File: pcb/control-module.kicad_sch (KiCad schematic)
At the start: 22 parts, among them J1 Screw_Terminal_01x06, J2 Conn_01x07_Pin, SW1 SW_DIP_x04, U1 TC2185-3.3VxCTTR

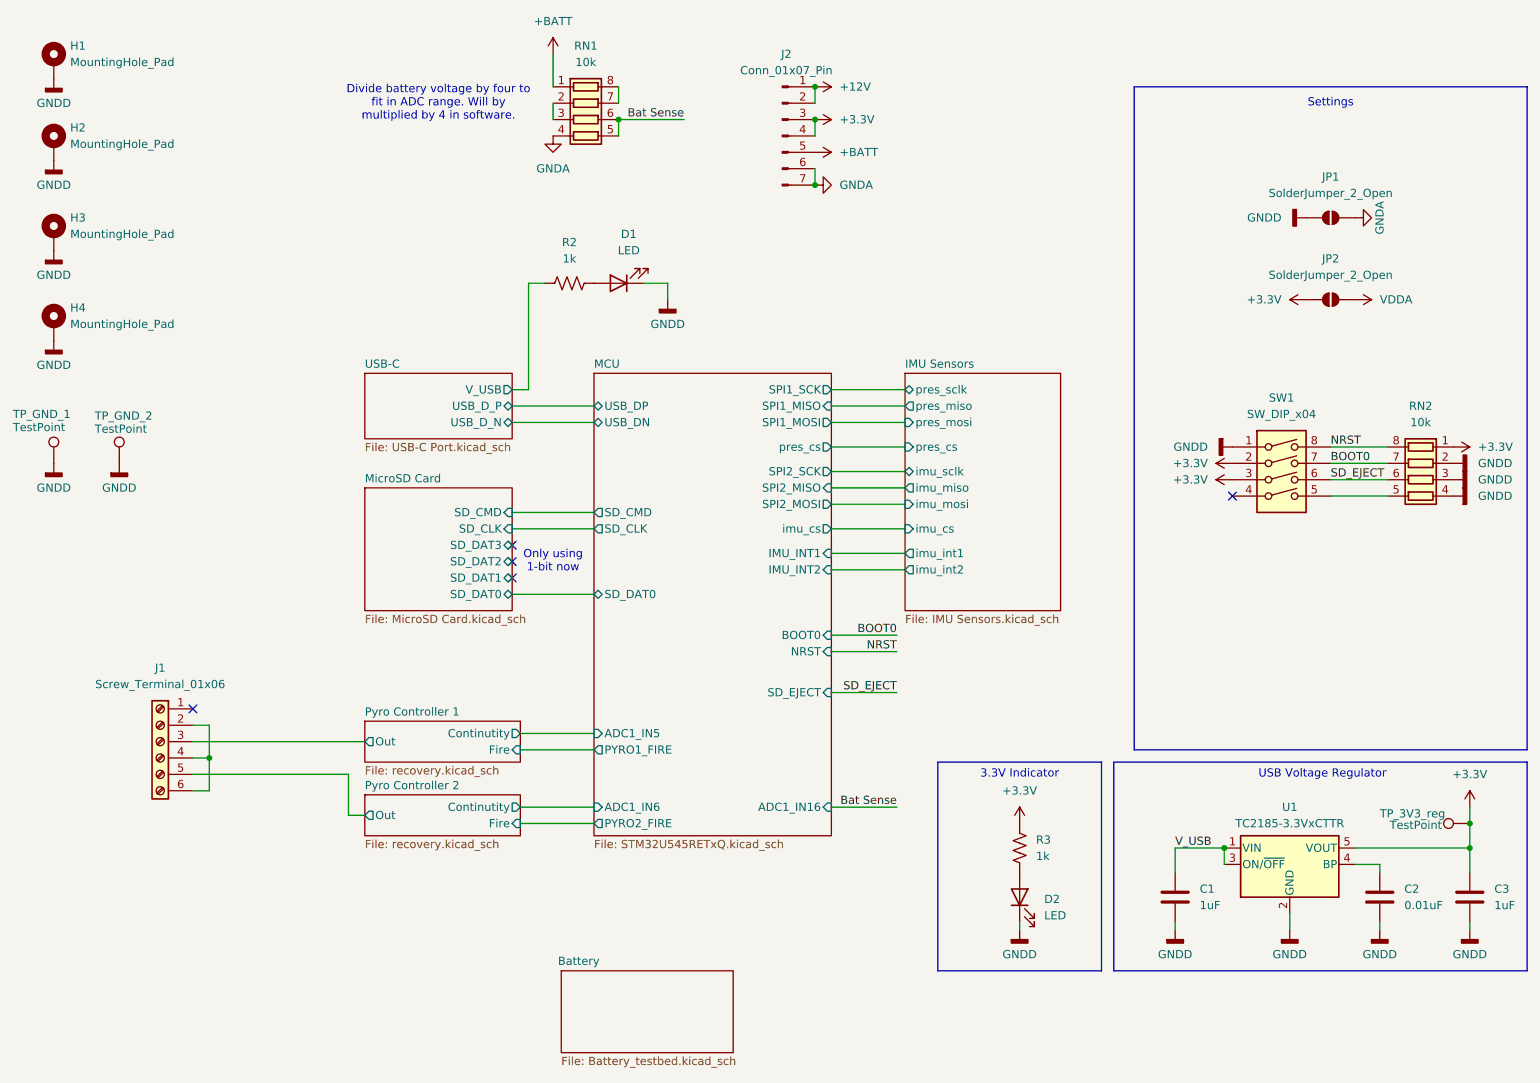
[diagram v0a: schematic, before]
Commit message: Updated Control Mod test bed schematics
finished testpoints, got rid of Vbus and replaced with +5V, added +3.3v to pyro J1 terminal
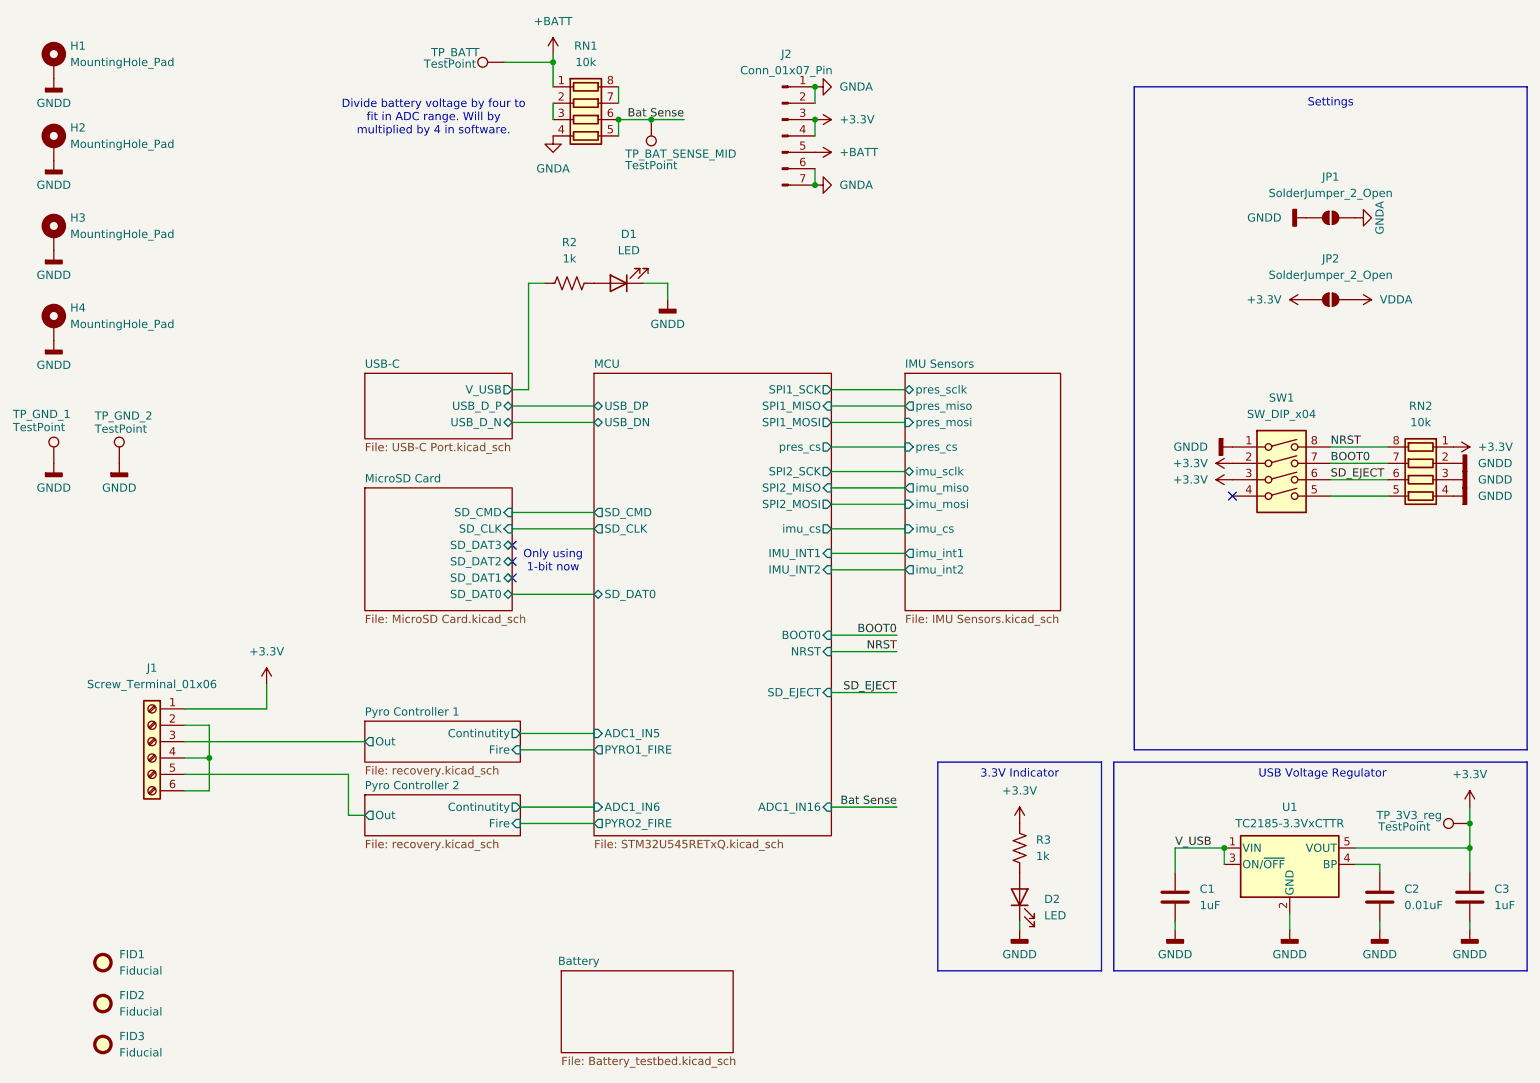
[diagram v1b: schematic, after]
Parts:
- added FID1, FID2, FID3: Fiducial, Fiducial:Fiducial_1mm_Mask2mm, symbol Mechanical:Fiducial
- added TP_BATT, TP_BAT_SENSE_MID: TestPoint, TestPoint:TestPoint_Loop_D2.54mm_Drill1.5mm_Beaded, symbol Connector:TestPoint
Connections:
- net +12V is gone; now on net GNDA: J2.1 (Pin_1), J2.2 (Pin_2)
- net +3.3V: now also J1.1 (Pin_1)
- net +BATT: now also TP_BATT.1
- net Bat Sense: now also TP_BAT_SENSE_MID.1
- no-connect marks 5 -> 4
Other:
- moved on the sheet: J1
